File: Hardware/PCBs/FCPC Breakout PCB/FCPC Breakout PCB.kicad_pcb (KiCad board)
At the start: 2 copper layers, 100.3 x 20 mm, 15 parts, among them J1 CAN, J10 RS485, J2 RS485, J3 UART, J4 5V, J5 12V, J6 UART, J7 CAN, J8 5V, J9 12V

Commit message: update
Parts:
- added kibuzzard-6696DEDD: G***, kibuzzard-6696DEDD, F.Cu at (127.0, 131.2)
- added kibuzzard-6696DEDD: G***, kibuzzard-6696DEDD, F.Cu at (115.6, 131.2)
- added kibuzzard-6696DEF0: G***, kibuzzard-6696DEF0, F.Cu at (112.0, 131.2)
- added kibuzzard-6696DF0D: G***, kibuzzard-6696DF0D, F.Cu at (123.4, 131.2)
- added kibuzzard-6696DF63: G***, kibuzzard-6696DF63, F.Cu at (157.0, 131.2)
- added kibuzzard-6696DF6D: G***, kibuzzard-6696DF6D, F.Cu at (153.5, 131.2)
- added kibuzzard-6696DFAD: G***, kibuzzard-6696DFAD, F.Cu at (181.5, 131.2)
- added kibuzzard-6696DFC0: G***, kibuzzard-6696DFC0, F.Cu at (185.0, 131.2)
- added kibuzzard-6696DFD9: G***, kibuzzard-6696DFD9, F.Cu at (188.5, 131.2)
- added kibuzzard-6696DFE7: G***, kibuzzard-6696DFE7, F.Cu at (192.0, 131.2)
- added kibuzzard-6696E01E: G***, kibuzzard-6696E01E, F.Cu at (164.0, 131.2)
- added kibuzzard-6696E02F: G***, kibuzzard-6696E02F, F.Cu at (167.6, 131.2)
- added kibuzzard-6696E03F: G***, kibuzzard-6696E03F, F.Cu at (171.2, 131.2)
- added kibuzzard-6696E054: G***, kibuzzard-6696E054, F.Cu at (174.7, 131.2)

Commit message: FPCP Breakout PCB Update:
B - L to B - H on error fix on silk screen
V 1.1 Board created
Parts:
- removed kibuzzard-6696DFE7: G***, kibuzzard-6696DFE7
- added kibuzzard-66AD0A40: G***, kibuzzard-66AD0A40, F.Cu at (192.0, 131.2)
- added kibuzzard-66AD0A64: G***, kibuzzard-66AD0A64, F.Cu at (139.9, 125.9)

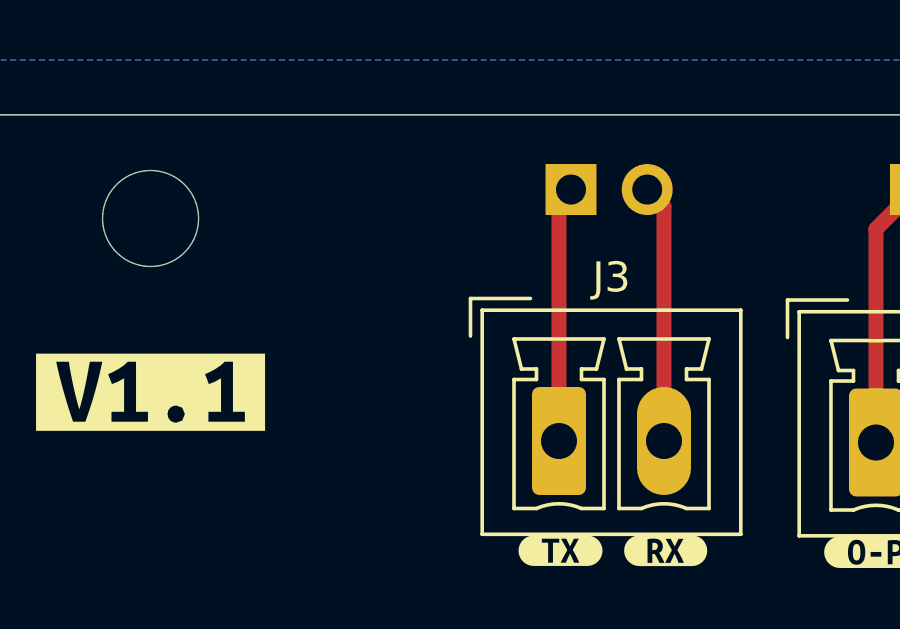
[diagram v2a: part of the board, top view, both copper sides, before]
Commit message: PCB Update
UART Voltage Divider 5V -> 3.3V
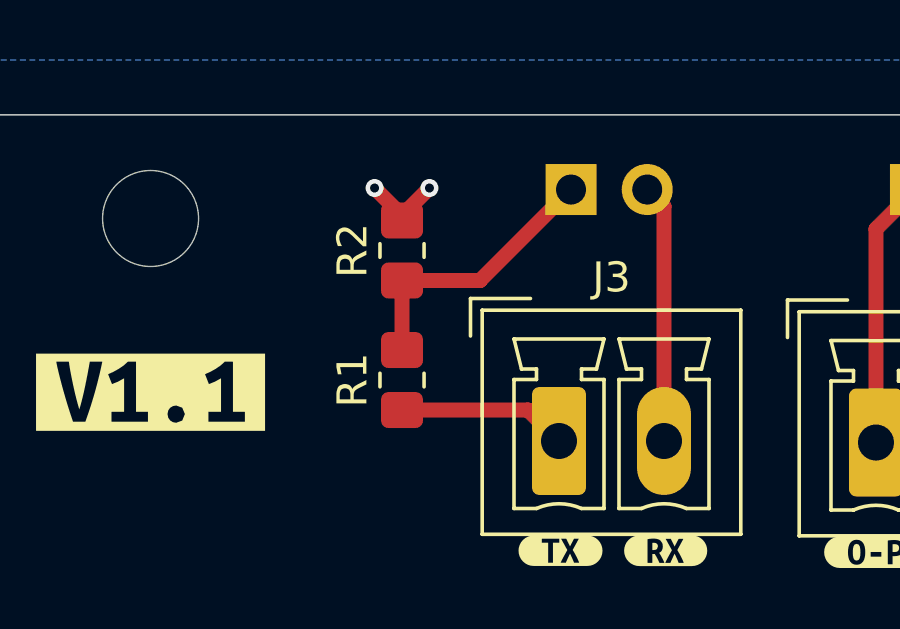
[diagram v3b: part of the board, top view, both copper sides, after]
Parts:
- added R1: 470, Resistor_SMD:R_0805_2012Metric_Pad1.20x1.40mm_HandSolder, F.Cu at (148.2, 125.5)
- added R2: 1K, Resistor_SMD:R_0805_2012Metric_Pad1.20x1.40mm_HandSolder, F.Cu at (148.2, 121.2)
- C1, C2: value 10uF -> C
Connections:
- J6 pad 1: UART TX -> UART TX 3.3V
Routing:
- net UART TX 3.3V: track 0.00 -> 9.26 mm
- net UART TX: track 8.55 -> 5.66 mm
- net GND: track 2.80 -> 5.56 mm, vias 2 -> 4
